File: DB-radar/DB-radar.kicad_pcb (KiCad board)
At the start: 2 copper layers, 60 x 60 mm, 67 parts, among them J1 USB_C_Receptacle, J2 Conn_01x10_Female, Q1 FS8205A, Q2 PN2222A, Q3 PN2222A, SW1 SW_Push, U1 ATmega328PB-A, U2 DW01A-G, U3 TP4056, U4 XC6206PxxxMR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

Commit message: De fleste komponenter plassert
Mangler bare et par blokker og routing
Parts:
- removed D2: LED, LED_SMD:LED_0805_2012Metric
- removed R8: 1k, Resistor_SMD:R_0603_1608Metric
- removed pre_bat_prog1: SW_Push, Jumper:SolderJumper-2_P1.3mm_Bridged2Bar_RoundedPad1.0x1.5mm
- added SW2: SW_SPDT, fish_watch:MSK-12C02, B.Cu at (117.9, 110.7)
- added SW4: SW_MEC_5G, Jumper:SolderJumper-2_P1.3mm_Open_TrianglePad1.0x1.5mm, B.Cu at (95.0, 142.7)
- J1, J2, R1, R2, SW1: moved to B.Cu
- R10: footprint Resistor_SMD:R_0603_1608Metric -> Resistor_SMD:R_0805_2012Metric_Pad1.20x1.40mm_HandSolder
- moved Q1 195.8 mm to (104.0, 117.0)
- moved U2 192.3 mm to (95.1, 117.0)
- moved R9 190.9 mm to (92.3, 117.8), turned to 90 degrees
- moved U3 183.4 mm to (107.7, 104.1), turned to 75 degrees
- moved C2 178.2 mm to (97.9, 116.2), turned to 90 degrees
- moved R10 174.2 mm to (107.2, 112.8), turned to 90 degrees
- moved R7 173.3 mm to (98.7, 111.8)
- moved C4 165.2 mm to (107.5, 109.0), turned to 165 degrees
- moved D1 159.5 mm to (101.6, 112.7), turned to 90 degrees
- moved R6 158.9 mm to (111.8, 103.1), turned to 75 degrees
- moved C3 82.8 mm to (169.2, 76.2)
- moved C10 82.4 mm to (107.7, 141.7)
- moved C9 81.9 mm to (107.7, 138.7)
- moved R11 79.6 mm to (107.7, 140.2)
- moved D26 76.5 mm to (84.0, 137.2), turned to -150 degrees
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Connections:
- C7 pad 2: VCC -> VCC_bat
- C8 pad 2: VCC -> VCC_bat
- U3 pad 6: Net-(D2-K) -> unconnected-(U3-~{STDBY}-Pad6)
- U4 pad 2: VCC -> VCC_bat
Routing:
- net Net-(D19-A): track 0.00 -> 32.6 mm
- net Net-(D27-A): track 0.00 -> 32.6 mm
- net Net-(D23-A): track 0.00 -> 32.6 mm
- net Net-(U1-XTAL2/PB7): track 0.00 -> 5.66 mm
- net Net-(U1-XTAL1/PB6): track 0.00 -> 5.55 mm
- net GND: track 0.00 -> 3.06 mm
- net Net-(U1-AREF): track 0.00 -> 2.84 mm
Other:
- board text added: "Battery or USB (Depending SW4)"
- board text added: "Programming header"

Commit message: Begynnt å route
Mega-rotete
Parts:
- BT1, C3, Q2, R12, R13, R5, U6, U7: moved to B.Cu
- moved U8 97.3 mm to (96.1, 137.6), turned to 90 degrees
- moved U6 92.5 mm to (80.3, 132.1), turned to -165 degrees
- moved C3 91.5 mm to (84.0, 109.5), turned to 45 degrees
- moved BT1 91.2 mm to (87.3, 112.8), turned to 45 degrees
- moved Q3 83.0 mm to (88.9, 113.9), turned to -90 degrees
- moved R3 77.8 mm to (88.9, 118.0), turned to 90 degrees
- moved U5 74.5 mm to (89.4, 123.4), turned to 90 degrees
- moved U7 72.1 mm to (115.8, 127.0), turned to 180 degrees
- moved R14 71.5 mm to (92.3, 112.8)
- moved Q2 64.6 mm to (125.5, 125.0), turned to 180 degrees
- moved R12 57.0 mm to (121.7, 125.0)
- moved R5 56.6 mm to (104.8, 108.2), turned to 180 degrees
- moved R13 50.2 mm to (125.7, 121.9), turned to 180 degrees
- moved U4 48.8 mm to (115.2, 127.9), turned to 90 degrees
- moved C6 40.8 mm to (114.7, 124.4), turned to -90 degrees
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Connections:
- SW2 pad 1: VCC_prog -> VCC_bat
- SW2 pad 3: VCC_bat -> VCC_prog
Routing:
- net VCC: track 0.00 -> 129.9 mm, vias 0 -> 4
- net VCC_prog: track 0.00 -> 91.7 mm, vias 0 -> 2
- net BAT+: track 0.00 -> 79.0 mm, vias 0 -> 2
- net Net-(D11-K): track 0.00 -> 65.7 mm, vias 0 -> 3
- net A: track 0.00 -> 46.2 mm, vias 0 -> 1
- net B: track 0.00 -> 43.2 mm, vias 0 -> 1
- net RX: track 0.00 -> 37.3 mm, vias 0 -> 1
- net TX: track 0.00 -> 32.8 mm, vias 0 -> 1
- net LED_PWM: track 0.00 -> 30.4 mm, vias 0 -> 1
- net MOSI: track 0.00 -> 28.6 mm, vias 0 -> 1
- net Net-(D10-K): track 0.00 -> 23.7 mm, vias 0 -> 1
- net -BATT: track 0.00 -> 23.5 mm, vias 0 -> 1
- net SCK: track 0.00 -> 23.2 mm, vias 0 -> 1
- net MISO: track 0.00 -> 23.0 mm, vias 0 -> 1
- net 5V: track 0.00 -> 19.6 mm
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
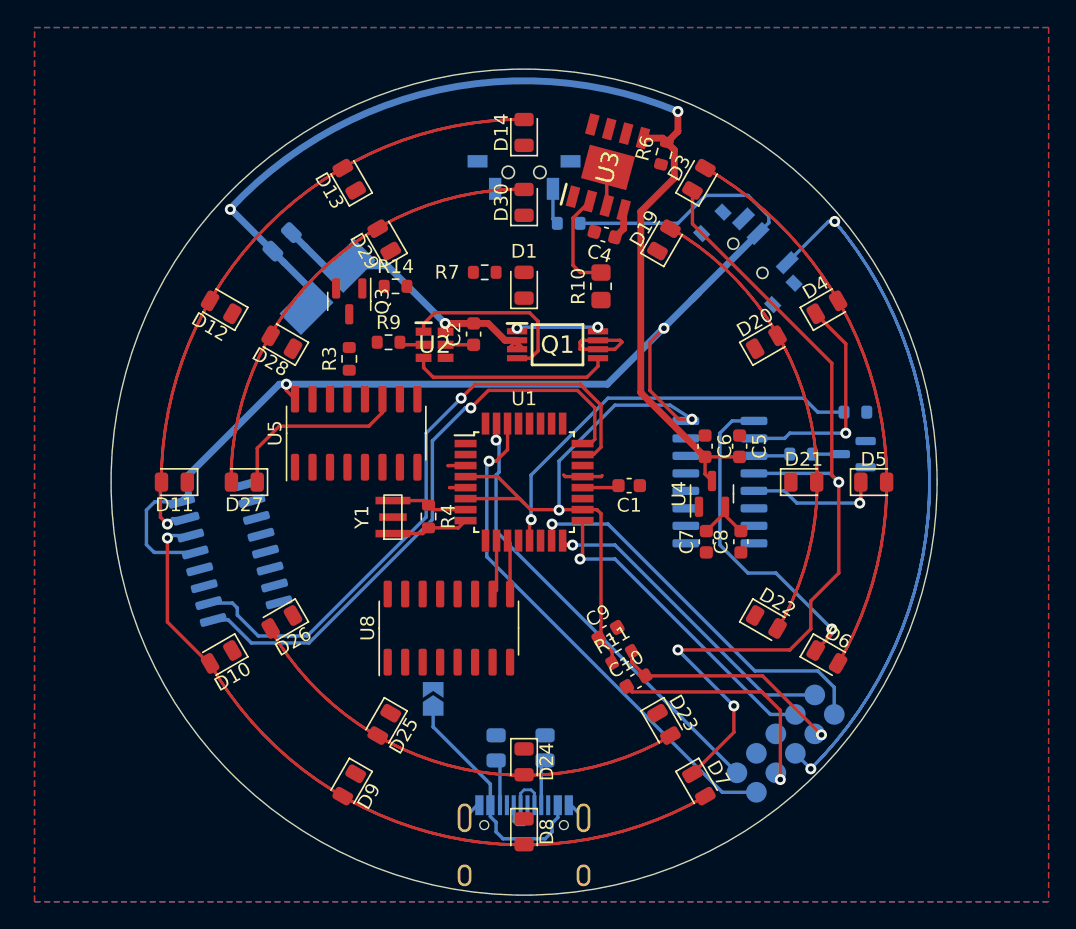
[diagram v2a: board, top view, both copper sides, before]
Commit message: Økte til 4 layers og routet ferdig
Har også kjørt DRC, og det eneste som gjenstår er en GND Zone som den påstår ikke er connected
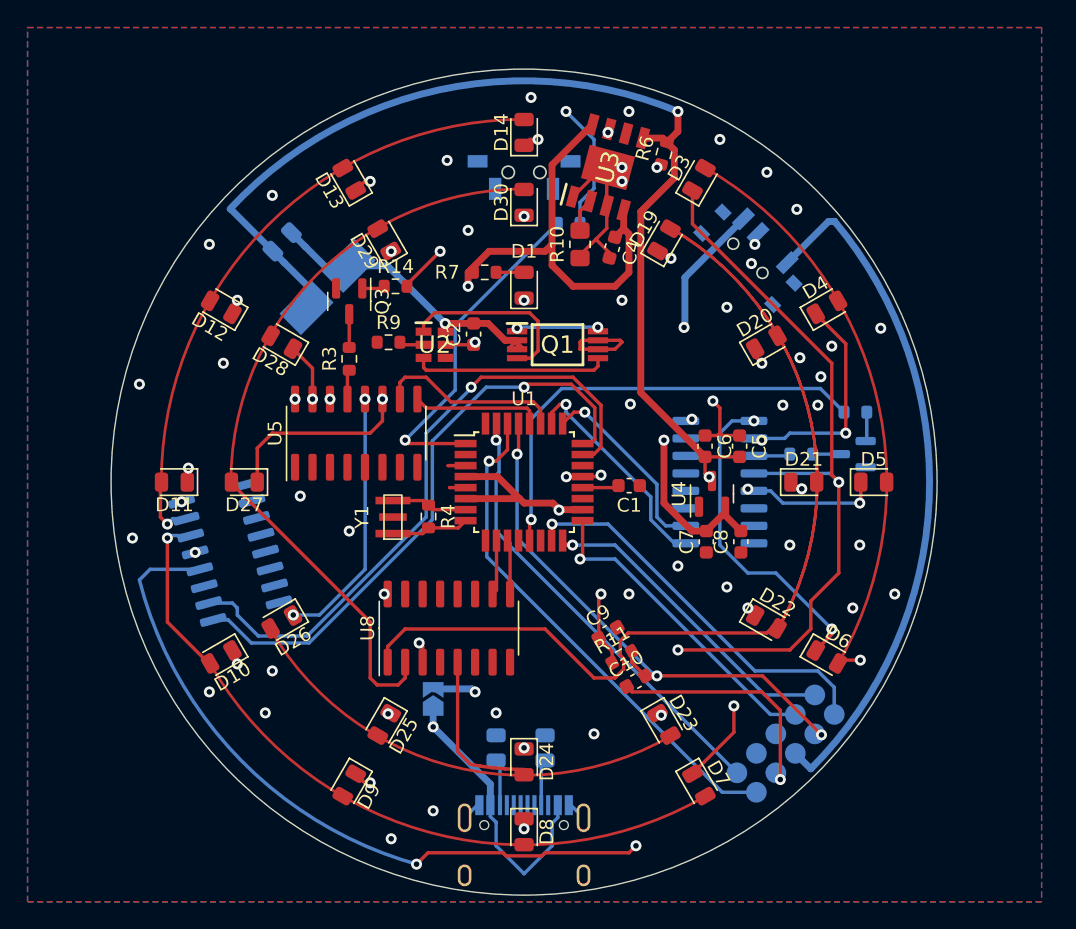
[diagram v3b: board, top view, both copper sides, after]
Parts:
- moved R10 3.41 mm to (105.7, 109.7)
- moved C4 1.10 mm to (108.0, 110.0), turned to -105 degrees
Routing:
- net VCC: track 129.9 -> 31.9 mm, vias 4 -> 11
- net Net-(D12-K): track 16.4 -> 112.9 mm, vias 1 -> 4
- net Net-(D13-K): track 9.61 -> 97.9 mm, vias 1 -> 4
- net Net-(D21-K): track 0.00 -> 83.1 mm, vias 0 -> 5
- net Net-(D10-K): track 23.7 -> 104.9 mm, vias 1 -> 4
- net Net-(D19-K): track 13.6 -> 94.3 mm, vias 0 -> 3
- net Net-(D20-K): track 0.00 -> 79.6 mm, vias 0 -> 3
- net Net-(D3-A): track 40.4 -> 115.3 mm, vias 0 -> 3
- net Net-(D22-K): track 0.00 -> 74.6 mm, vias 0 -> 4
- net 5V: track 19.6 -> 87.8 mm, vias 0 -> 2
- net LED_PWM: track 30.4 -> 93.0 mm, vias 1 -> 3
- net Net-(D11-K): track 65.7 -> 110.2 mm, vias 3 -> 4
- net Net-(D19-A): track 32.6 -> 66.9 mm
- net BAT+: track 79.0 -> 109.7 mm, vias 2 -> 3
- net VCC_bat: track 4.57 -> 31.6 mm, vias 0 -> 2
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- added copper zone on In1.Cu, net VCC
- added copper zone on In2.Cu, net VCC
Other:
- copper layers 2 -> 4

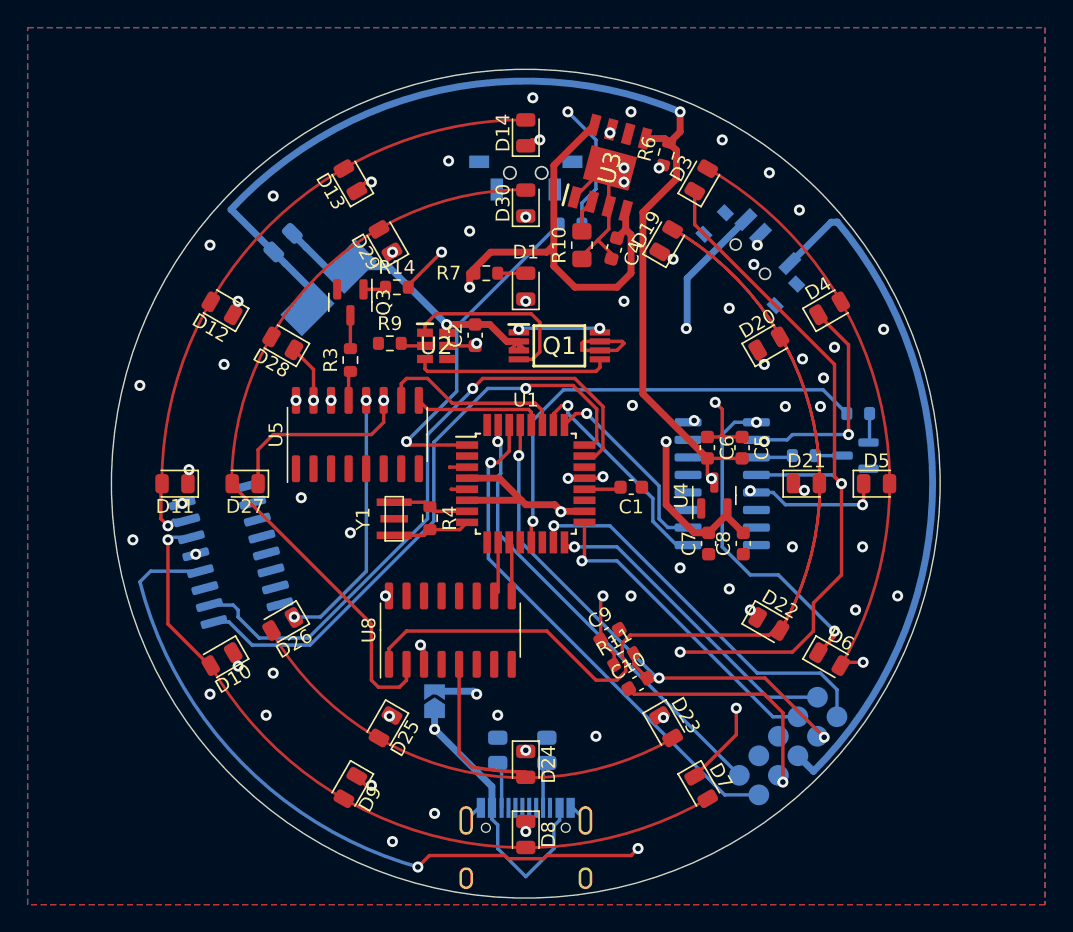
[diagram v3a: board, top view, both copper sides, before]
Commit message: Fulførte routing og passed DRC
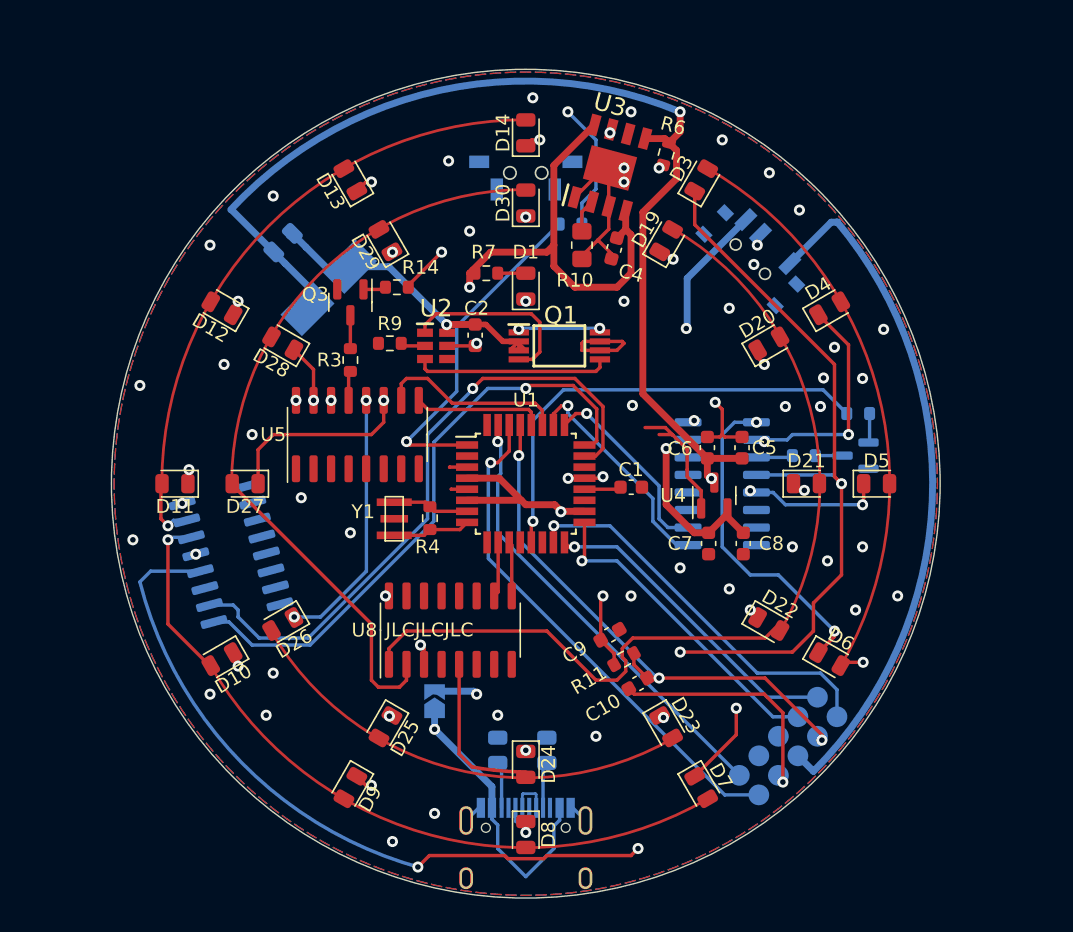
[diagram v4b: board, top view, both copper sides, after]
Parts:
- added G***: LOGO, LOGO, B.Cu at (100.6, 127.5)
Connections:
- SW2 pad S: (no net) -> GND
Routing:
- net GND: track 33.4 -> 42.8 mm, vias 40 -> 42
- net D-: track 0.00 -> 2.99 mm
- net D+: track 0.00 -> 2.99 mm
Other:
- board text added: "Designed by Iver Iscariot Søbakk"
- board text added: "Dragon ball radar - clock"
- board text added: "JLCJLCJLC"

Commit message: fikset silk bak
Byttet strøm-selector og SPI kommentarer
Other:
- board text added: "Vcc"
- board text added: "cts"
- board text added: "dtr"
- board text added: "gnd"
- board text added: "miso"
- board text added: "mosi"
- board text added: "reset"
- board text added: "rx"
- board text added: "sck"
- board text added: "tx"
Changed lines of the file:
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@@
   (gr_circle (center 101.6 127) (end 131.6 127)
     (stroke (width 0.1) (type default)) (fill none) (layer "Edge.Cuts"))
+  (gr_text "tx" (at 115.640545 149.541138) (layer "B.SilkS")
+    (effects (font (size 1 1) (thickness 0.15)) (justify left bottom mirror))
+  )
+  (gr_text "sck" (at 118.639688 140.787391) (layer "B.SilkS")
+    (effects (font (size 1 1) (thickness 0.15)) (justify left bottom mirror))
+  )
+  (gr_text "dtr" (at 116.877692 145.960912) (layer "B.SilkS")
+    (effects (font (size 1 1) (thickness 0.15)) (justify left bottom mirror))
+  )
   (gr_text "Dragon ball radar - clock" (at 99.06 98.044 30) (layer "B.SilkS")
     (effects (font (size 1.2 1.2) (thickness 0.15)) (justify left bottom mirror))
   )
-  (gr_text "Programming\nheader" (at 113.284 112.268 315) (layer "B.SilkS")
+  (gr_text "gnd" (at 116.259118 142.193239) (layer "B.SilkS")
+    (effects (font (size 1 1) (thickness 0.15)) (justify left bottom mirror))
+  )
+  (gr_text "Programming\nheader" (at 116.619649 114.867228 315) (layer "B.SilkS")
+    (effects (font (size 0.7 0.7) (thickness 0.125) bold) (justify right bottom mirror))
+  )
+  (gr_text "rx" (at 117.065138 151.2469) (layer "B.SilkS")
+    (effects (font (size 1 1) (thickness 0.15)) (justify left bottom mirror))
+  )
+  (gr_text "reset" (at 121.132725 142.380686) (layer "B.SilkS")
+    (effects (font (size 1 1) (thickness 0.15)) (justify left bottom mirror))
+  )
+  (gr_text "Battery or USB\n(Depending SW4)" (at 113.456491 111.914947 315) (layer "B.SilkS")
     (effects (font (size 0.7 0.7) (thickness 0.125) bold) (justify left bottom mirror))
   )
-  (gr_text "Battery or USB\n(Depending SW4)" (at 116.332 114.808 315) (layer "B.SilkS")
-    (effects (font (size 0.7 0.7) (thickness 0.125) bold) (justify right bottom mirror))
+  (gr_text "cts" (at 115.265653 143.861512) (layer "B.SilkS")
+    (effects (font (size 1 1) (thickness 0.15)) (justify left bottom mirror))
+  )
+  (gr_text "mosi" (at 123.73823 141.068561) (layer "B.SilkS")
+    (effects (font (size 1 1) (thickness 0.15)) (justify left bottom mirror))
+  )
+  (gr_text "miso\n" (at 122.013723 139.512756) (layer "B.SilkS")
+    (effects (font (size 1 1) (thickness 0.15)) (justify left bottom mirror))
   )
   (gr_text "Designed by Iver Iscariot Søbakk" (at 99.822 99.363823 30) (layer "B.SilkS")
     (effects (font (size 0.9 0.9) (thickness 0.15)) (justify left bottom mirror))
+  )
+  (gr_text "Vcc" (at 118.733411 144.311384) (layer "B.SilkS")
+    (effects (font (size 1 1) (thickness 0.15)) (justify left bottom mirror))
   )
   (gr_text "JLCJLCJLC" (at 91.44 138.176) (layer "F.SilkS")
@@
         (xy 131.324121 129.175525)
         (xy 131.383745 128.088489)
-        (xy 131.403629 127)
       )
     )
